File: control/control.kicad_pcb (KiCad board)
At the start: 4 copper layers, 45.7 x 39.4 mm, 90 parts, among them M1 LMR62014, M2 LM46001, M3 STM32F4XX, M4 TPS736XX, M5 SN65HVD23X, P1 GND/VDD, P2 VOLTAGE, P3 INTERFACE, P4 POWER/FETS, P5 SENSOR_A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

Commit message: Added separate +5v polygon on control board.
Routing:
- net +5V: track 67.3 -> 71.3 mm, vias 1 -> 5
- net +3.3V: track 72.8 -> 70.7 mm, vias 15 -> 14
- added copper zone on In2.Cu, net +5V
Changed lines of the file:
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@@
     (links 215)
     (no_connects 0)
-    (area 96.4311 52.395 155.955 99.770001)
+    (area 97.079999 60.249999 142.950001 99.770001)
     (thickness 1.6)
     (drawings 7)
-    (tracks 718)
+    (tracks 723)
     (zones 0)
     (modules 90)
@@
   (title_block
     (title "Phobia Control Board")
-    (date 2016-03-25)
+    (date 2016-03-31)
     (rev 2)
     (company "Roman Belov")
@@
   )
   (setup
-    (last_trace_width 1.016)
+    (last_trace_width 0.889)
     (user_trace_width 0.381)
     (user_trace_width 0.508)
@@
       (net 72 EN_A))
   )
-  (gr_text r2 (at 108.585 97.155) (layer B.Cu)
-    (effects (font (size 1.5 1.5) (thickness 0.3)) (justify mirror))
+  (gr_text r2 (at 116.205 82.55 360) (layer F.Cu)
+    (effects (font (size 1.5 1.5) (thickness 0.3)))
   )
   (dimension 39.37 (width 0.3) (layer Eco1.User)
@@
   (gr_line (start 142.875 60.325) (end 142.875 99.695) (layer Edge.Cuts) (width 0.15))
   (gr_line (start 97.155 60.325) (end 142.875 60.325) (layer Edge.Cuts) (width 0.15))
+  (segment (start 111.76 81.28) (end 106.68 81.28) (width 0.889) (layer F.Cu) (net 1))
+  (segment (start 111.76 81.28) (end 111.76 78.867) (width 0.889) (layer F.Cu) (net 1))
+  (segment (start 112.395 81.28) (end 111.76 81.28) (width 0.889) (layer F.Cu) (net 1))
+  (via (at 111.76 81.28) (size 0.7) (drill 0.3) (layers F.Cu B.Cu) (net 1))
+  (segment (start 113.03 81.28) (end 112.395 81.28) (width 0.889) (layer F.Cu) (net 1))
+  (via (at 112.395 81.28) (size 0.7) (drill 0.3) (layers F.Cu B.Cu) (net 1))
+  (segment (start 113.665 81.28) (end 113.03 81.28) (width 0.889) (layer F.Cu) (net 1))
+  (via (at 113.03 81.28) (size 0.7) (drill 0.3) (layers F.Cu B.Cu) (net 1))
+  (segment (start 113.792 78.74) (end 113.792 81.153) (width 0.889) (layer F.Cu) (net 1))
+  (segment (start 113.792 81.153) (end 113.665 81.28) (width 0.889) (layer F.Cu) (net 1))
+  (via (at 113.665 81.28) (size 0.7) (drill 0.3) (layers F.Cu B.Cu) (net 1))
+  (segment (start 111.76 78.867) (end 111.633 78.74) (width 0.889) (layer F.Cu) (net 1))
   (segment (start 102.235 83.312) (end 100.457 83.312) (width 0.889) (layer B.Cu) (net 1))
   (segment (start 100.457 83.312) (end 100.33 83.185) (width 0.889) (layer B.Cu) (net 1))
@@
   (segment (start 100.035001 71.079001) (end 103.018201 71.079001) (width 0.508) (layer F.Cu) (net 1))
   (segment (start 103.155 70.942202) (end 103.155 70.125) (width 0.508) (layer F.Cu) (net 1))
-  (segment (start 106.68 81.28) (end 111.506 81.28) (width 0.889) (layer F.Cu) (net 1))
-  (segment (start 111.633 81.153) (end 111.633 78.74) (width 0.889) (layer F.Cu) (net 1))
-  (segment (start 111.506 81.28) (end 111.633 81.153) (width 0.889) (layer F.Cu) (net 1))
   (segment (start 101.6 82.9945) (end 101.6 81.28) (width 0.889) (layer F.Cu) (net 1))
   (segment (start 101.6 81.28) (end 106.68 81.28) (width 0.889) (layer F.Cu) (net 1))
@@
   (segment (start 100.5205 82.9945) (end 100.33 83.185) (width 1.016) (layer F.Cu) (net 1))
   (segment (start 99.06 81.28) (end 101.6 81.28) (width 0.889) (layer F.Cu) (net 1))
-  (segment (start 111.633 79.502) (end 111.633 78.74) (width 0.889) (layer F.Cu) (net 1))
   (segment (start 98.288499 80.508499) (end 99.06 81.28) (width 0.889) (layer F.Cu) (net 1))
   (segment (start 99.695 70.739) (end 99.5045 70.739) (width 0.889) (layer F.Cu) (net 1))
@@
   (segment (start 127.4445 78.74) (end 127.4445 80.01) (width 0.508) (layer B.Cu) (net 3))
   (segment (start 127.4445 80.01) (end 128.0795 80.645) (width 0.508) (layer B.Cu) (net 3))
-  (via (at 114.3 83.185) (size 0.7) (drill 0.3) (layers F.Cu B.Cu) (net 3))
-  (segment (start 113.792 83.693) (end 114.3 83.185) (width 0.508) (layer B.Cu) (net 3))
-  (segment (start 113.792 85.09) (end 113.792 83.693) (width 0.508) (layer B.Cu) (net 3))
   (segment (start 135.89 95.6945) (end 135.89 94.615) (width 0.508) (layer F.Cu) (net 3))
   (via (at 135.89 94.615) (size 0.7) (drill 0.3) (layers F.Cu B.Cu) (net 3))
@@
   (via (at 115.57 80.01) (size 0.7) (drill 0.3) (layers F.Cu B.Cu) (net 61))
   (segment (start 109.855 78.105) (end 109.855 77.47) (width 0.508) (layer F.Cu) (net 61))
-  (via (at 109.855 77.47) (size 0.7) (drill 0.3) (layers F.Cu B.Cu) (net 61))
-  (segment (start 109.855 78.74) (end 109.855 78.105) (width 0.508) (layer B.Cu) (net 61))
-  (via (at 109.855 78.105) (size 0.7) (drill 0.3) (layers F.Cu B.Cu) (net 61))
-  (segment (start 109.855 79.375) (end 109.855 78.74) (width 0.508) (layer F.Cu) (net 61))
-  (via (at 109.855 78.74) (size 0.7) (drill 0.3) (layers F.Cu B.Cu) (net 61))
-  (segment (start 109.855 80.01) (end 109.855 79.375) (width 0.508) (layer B.Cu) (net 61))
-  (via (at 109.855 79.375) (size 0.7) (drill 0.3) (layers F.Cu B.Cu) (net 61))
-  (segment (start 108.585 78.74) (end 109.855 80.01) (width 0.508) (layer F.Cu) (net 61))
   (via (at 109.855 80.01) (size 0.7) (drill 0.3) (layers F.Cu B.Cu) (net 61))
+  (segment (start 108.585 78.74) (end 109.855 80.01) (width 0.508) (layer F.Cu) (net 61))
+  (via (at 109.855 79.375) (size 0.7) (drill 0.3) (layers F.Cu B.Cu) (net 61))
+  (segment (start 109.855 80.01) (end 109.855 79.375) (width 0.508) (layer B.Cu) (net 61))
+  (via (at 109.855 78.74) (size 0.7) (drill 0.3) (layers F.Cu B.Cu) (net 61))
+  (segment (start 109.855 79.375) (end 109.855 78.74) (width 0.508) (layer F.Cu) (net 61))
+  (via (at 109.855 78.105) (size 0.7) (drill 0.3) (layers F.Cu B.Cu) (net 61))
+  (segment (start 109.855 78.74) (end 109.855 78.105) (width 0.508) (layer B.Cu) (net 61))
+  (via (at 109.855 77.47) (size 0.7) (drill 0.3) (layers F.Cu B.Cu) (net 61))
   (segment (start 109.855 74.295) (end 109.855 73.66) (width 0.508) (layer F.Cu) (net 61))
   (via (at 109.855 73.66) (size 0.7) (drill 0.3) (layers F.Cu B.Cu) (net 61))
@@
     (polygon
       (pts
-        (xy 114.935 67.945) (xy 116.84 67.945) (xy 116.84 70.485) (xy 114.3 73.025) (xy 114.3 80.645)
-        (xy 111.125 80.645) (xy 111.125 72.39) (xy 114.935 68.58)
+        (xy 114.935 67.945) (xy 116.84 67.945) (xy 116.84 70.485) (xy 114.3 73.025) (xy 114.3 81.915)
+        (xy 111.125 81.915) (xy 111.125 72.39) (xy 114.935 68.58)
       )
     )
@@
       )
     )
+  )
+  (zone (net 1) (net_name +5V) (layer In2.Cu) (hatch edge 0.508)
+    (priority 1)
+    (connect_pads (clearance 0.254))
+    (min_thickness 0.254)
+    (fill yes (arc_segments 16) (thermal_gap 0.508) (thermal_bridge_width 0.508))
+    (polygon
+      (pts
+        (xy 97.79 60.96) (xy 109.22 60.96) (xy 118.11 69.85) (xy 118.11 81.28) (xy 114.3 85.09)
+        (xy 107.95 85.09) (xy 106.68 86.36) (xy 106.68 92.329) (xy 103.886 95.123) (xy 103.886 99.06)
+        (xy 97.79 99.06)
+      )
+    )

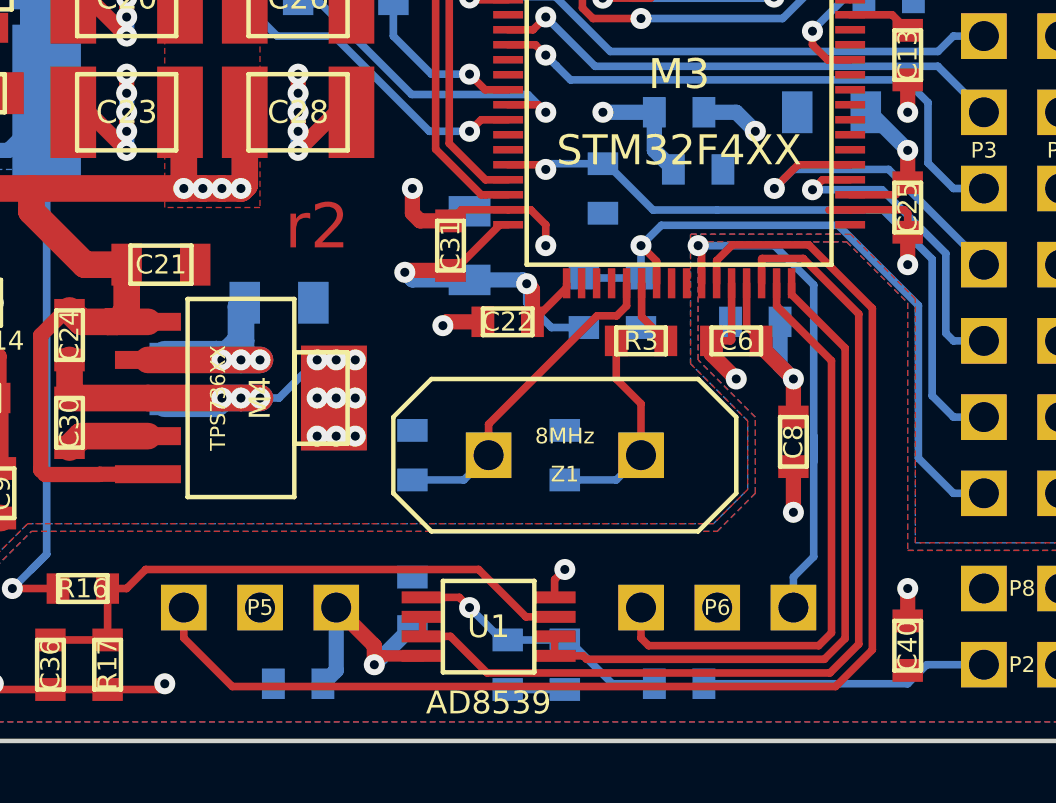
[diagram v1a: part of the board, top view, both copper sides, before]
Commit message: Replaced ACS7XX sensors to the current shunt amplifiers.
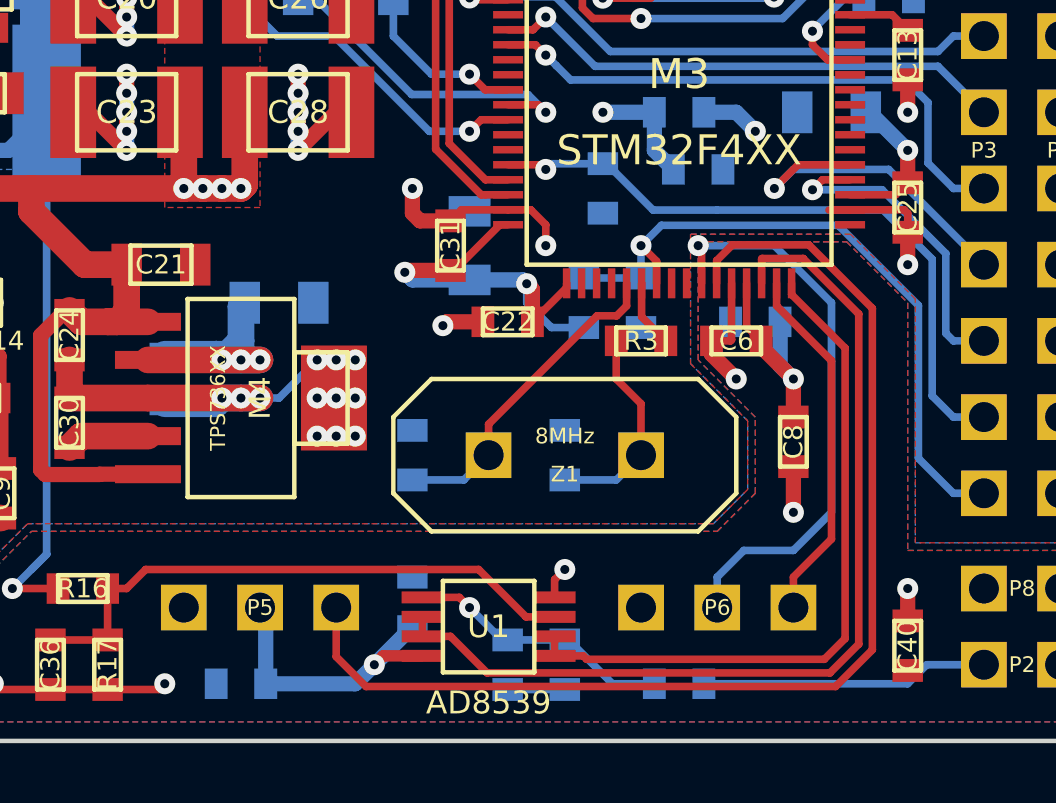
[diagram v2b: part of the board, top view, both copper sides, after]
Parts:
- moved C43 1.90 mm to (113.7, 97.8)
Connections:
- P5 pad 1: ADC_IN13 -> GND
- P5 pad 2: GND -> +3.3V
- P5 pad 3: +3.3V -> ADC_IN13
- P6 pad 1: ADC_IN1 -> GND
- P6 pad 2: GND -> ADC_IN12
- P6 pad 3: ADC_IN12 -> ADC_IN1
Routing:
- net ADC_IN1: track 20.1 -> 12.1 mm
- net ADC_IN13: track 43.6 -> 39.1 mm
- net ADC_IN12: track 17.6 -> 19.2 mm
- net +3.3V: track 70.7 -> 72.0 mm
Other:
- board text removed: "r2"
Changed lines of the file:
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@@
-(kicad_pcb (version 4) (host pcbnew 4.0.1-stable)
+(kicad_pcb (version 4) (host pcbnew 4.0.2-stable)
   (general
     (links 215)
@@
     (area 97.079999 60.249999 142.950001 99.770001)
     (thickness 1.6)
-    (drawings 7)
-    (tracks 723)
+    (drawings 6)
+    (tracks 722)
     (zones 0)
     (modules 90)
@@
   )
   (setup
-    (last_trace_width 0.889)
+    (last_trace_width 0.508)
     (user_trace_width 0.381)
     (user_trace_width 0.508)
@@
     )
     (pad 1 thru_hole rect (at -2.54 0) (size 1.524 1.524) (drill 1) (layers *.Cu *.Mask)
+      (net 61 GND))
+    (pad 3 thru_hole rect (at 2.54 0) (size 1.524 1.524) (drill 1) (layers *.Cu *.Mask)
       (net 68 ADC_IN13))
-    (pad 3 thru_hole rect (at 2.54 0) (size 1.524 1.524) (drill 1) (layers *.Cu *.Mask)
-      (net 3 +3.3V))
     (pad 2 thru_hole rect (at 0 0) (size 1.524 1.524) (drill 1) (layers *.Cu *.Mask)
-      (net 61 GND))
+      (net 3 +3.3V))
   )
   (module foot:PLS3 (layer F.Cu)
@@
     )
     (pad 1 thru_hole rect (at -2.54 0) (size 1.524 1.524) (drill 1) (layers *.Cu *.Mask)
+      (net 61 GND))
+    (pad 3 thru_hole rect (at 2.54 0) (size 1.524 1.524) (drill 1) (layers *.Cu *.Mask)
       (net 32 ADC_IN1))
-    (pad 3 thru_hole rect (at 2.54 0) (size 1.524 1.524) (drill 1) (layers *.Cu *.Mask)
+    (pad 2 thru_hole rect (at 0 0) (size 1.524 1.524) (drill 1) (layers *.Cu *.Mask)
       (net 70 ADC_IN12))
-    (pad 2 thru_hole rect (at 0 0) (size 1.524 1.524) (drill 1) (layers *.Cu *.Mask)
-      (net 61 GND))
   )
   (module foot:PLS2 (layer F.Cu)
@@
   )
   (module foot:SM0603 (layer B.Cu)
-    (at 115.57 97.79 180)
+    (at 113.665 97.79 180)
     (attr smd)
     (fp_text reference C43 (at 0 0 180) (layer B.SilkS)
@@
     (pad 2 thru_hole rect (at -8.89 0 270) (size 1.524 1.524) (drill 1) (layers *.Cu *.Mask)
       (net 72 EN_A))
-  )
-  (gr_text r2 (at 116.205 82.55 360) (layer F.Cu)
-    (effects (font (size 1.5 1.5) (thickness 0.3)))
   )
   (dimension 39.37 (width 0.3) (layer Eco1.User)
@@
   (segment (start 109.22 65.151) (end 109.22 62.23) (width 1.016) (layer B.Cu) (net 2))
   (segment (start 107.188 67.183) (end 109.22 65.151) (width 1.016) (layer B.Cu) (net 2))
+  (segment (start 114.4905 97.79) (end 117.475 97.79) (width 0.508) (layer B.Cu) (net 3))
+  (segment (start 117.475 97.79) (end 118.11 97.155) (width 0.508) (layer B.Cu) (net 3))
+  (segment (start 114.4905 97.79) (end 114.4905 95.4405) (width 0.508) (layer B.Cu) (net 3))
+  (segment (start 114.4905 95.4405) (end 114.3 95.25) (width 0.508) (layer B.Cu) (net 3))
+  (segment (start 114.4905 95.4405) (end 114.3 95.25) (width 0.508) (layer F.Cu) (net 3))
   (segment (start 127.4445 78.74) (end 127.4445 80.01) (width 0.508) (layer B.Cu) (net 3))
   (segment (start 127.4445 80.01) (end 128.0795 80.645) (width 0.508) (layer B.Cu) (net 3))
@@
   (segment (start 119.72 96.86) (end 118.405 96.86) (width 0.381) (layer F.Cu) (net 3))
   (segment (start 118.405 96.86) (end 118.11 97.155) (width 0.381) (layer F.Cu) (net 3))
-  (segment (start 118.11 97.155) (end 118.11 96.52) (width 0.508) (layer F.Cu) (net 3))
-  (segment (start 118.11 96.52) (end 116.84 95.25) (width 0.508) (layer F.Cu) (net 3))
   (segment (start 123.19 85.09) (end 123.19 84.455) (width 0.254) (layer B.Cu) (net 3))
   (segment (start 124.0155 85.9155) (end 123.19 85.09) (width 0.254) (layer B.Cu) (net 3))
@@
   (segment (start 131.6355 85.725) (end 131.6355 87.1855) (width 0.508) (layer B.Cu) (net 3))
   (segment (start 131.6355 87.1855) (end 132.08 87.63) (width 0.508) (layer B.Cu) (net 3))
-  (segment (start 116.84 95.25) (end 116.84 97.3455) (width 0.508) (layer B.Cu) (net 3))
-  (segment (start 116.84 97.3455) (end 116.3955 97.79) (width 0.508) (layer B.Cu) (net 3))
   (segment (start 113.665 86.995) (end 113.665 86.36) (width 0.889) (layer B.Cu) (net 3))
   (segment (start 113.665 86.36) (end 113.665 85.217) (width 0.889) (layer B.Cu) (net 3))
@@
   (segment (start 132.08 87.63) (end 132.08 88.9) (width 0.508) (layer F.Cu) (net 3))
   (via (at 132.08 87.63) (size 0.7) (drill 0.3) (layers F.Cu B.Cu) (net 3))
-  (segment (start 117.0305 95.0595) (end 116.84 95.25) (width 0.508) (layer F.Cu) (net 3))
   (segment (start 121.285 84.328) (end 123.063 84.328) (width 0.508) (layer B.Cu) (net 3))
   (segment (start 123.063 84.328) (end 123.19 84.455) (width 0.508) (layer B.Cu) (net 3))
@@
   (segment (start 127.8255 86.36) (end 127.02 85.5545) (width 0.254) (layer F.Cu) (net 29))
   (segment (start 127.02 85.5545) (end 127.02 84.44) (width 0.254) (layer F.Cu) (net 29))
-  (segment (start 133.35 96.092602) (end 133.35 87.024) (width 0.254) (layer F.Cu) (net 32))
-  (segment (start 133.35 87.024) (end 131.52 85.194) (width 0.254) (layer F.Cu) (net 32))
-  (segment (start 131.52 85.194) (end 131.52 84.44) (width 0.254) (layer F.Cu) (net 32))
-  (segment (start 127.254 96.52) (end 132.922602 96.52) (width 0.254) (layer F.Cu) (net 32))
-  (segment (start 132.922602 96.52) (end 133.35 96.092602) (width 0.254) (layer F.Cu) (net 32))
-  (segment (start 127 95.25) (end 127 96.266) (width 0.254) (layer F.Cu) (net 32))
-  (segment (start 127 96.266) (end 127.254 96.52) (width 0.254) (layer F.Cu) (net 32))
+  (segment (start 133.35 87.024) (end 133.35 92.964) (width 0.254) (layer F.Cu) (net 32))
+  (segment (start 133.35 92.964) (end 132.08 94.234) (width 0.254) (layer F.Cu) (net 32))
+  (segment (start 132.08 94.234) (end 132.08 95.25) (width 0.254) (layer F.Cu) (net 32))
+  (segment (start 131.52 84.44) (end 131.52 85.194) (width 0.254) (layer F.Cu) (net 32))
+  (segment (start 131.52 85.194) (end 133.35 87.024) (width 0.254) (layer F.Cu) (net 32))
   (segment (start 124.12 96.86) (end 124.12 96.21) (width 0.254) (layer F.Cu) (net 33))
   (segment (start 133.80401 96.280659) (end 133.110659 96.974009) (width 0.254) (layer F.Cu) (net 33))
@@
   (segment (start 126.0475 97.79) (end 124.587 96.3295) (width 0.254) (layer B.Cu) (net 67))
   (segment (start 124.587 96.3295) (end 124.46 96.3295) (width 0.254) (layer B.Cu) (net 67))
-  (segment (start 111.76 95.25) (end 111.76 96.266) (width 0.254) (layer F.Cu) (net 68))
-  (segment (start 111.76 96.266) (end 113.37603 97.88203) (width 0.254) (layer F.Cu) (net 68))
-  (segment (start 113.37603 97.88203) (end 133.486772 97.88203) (width 0.254) (layer F.Cu) (net 68))
-  (segment (start 133.486772 97.88203) (end 134.71203 96.656772) (width 0.254) (layer F.Cu) (net 68))
-  (segment (start 134.71203 96.656772) (end 134.71203 85.276361) (width 0.254) (layer F.Cu) (net 68))
-  (segment (start 134.71203 85.276361) (end 132.594658 83.158989) (width 0.254) (layer F.Cu) (net 68))
-  (segment (start 132.594658 83.158989) (end 130.047011 83.158989) (width 0.254) (layer F.Cu) (net 68))
-  (segment (start 130.047011 83.158989) (end 129.52 83.686) (width 0.254) (layer F.Cu) (net 68))
-  (segment (start 129.52 83.686) (end 129.52 84.44) (width 0.254) (layer F.Cu) (net 68))
+  (segment (start 133.486773 97.882029) (end 117.835067 97.882029) (width 0.254) (layer F.Cu) (net 68))
+  (segment (start 117.835067 97.882029) (end 116.84 96.886962) (width 0.254) (layer F.Cu) (net 68))
+  (segment (start 116.84 96.886962) (end 116.84 95.25) (width 0.254) (layer F.Cu) (net 68))
+  (segment (start 134.71203 85.276361) (end 134.71203 96.656773) (width 0.254) (layer F.Cu) (net 68))
+  (segment (start 134.71203 96.656773) (end 133.486773 97.882029) (width 0.254) (layer F.Cu) (net 68))
+  (segment (start 129.52 84.44) (end 129.52 83.686) (width 0.254) (layer F.Cu) (net 68))
+  (segment (start 129.52 83.686) (end 130.047011 83.158989) (width 0.254) (layer F.Cu) (net 68))
+  (segment (start 130.047011 83.158989) (end 132.594658 83.158989) (width 0.254) (layer F.Cu) (net 68))
+  (segment (start 132.594658 83.158989) (end 134.71203 85.276361) (width 0.254) (layer F.Cu) (net 68))
+  (segment (start 117.0305 95.0595) (end 116.84 95.25) (width 0.508) (layer F.Cu) (net 68))
   (segment (start 135.89 97.79) (end 136.525 97.155) (width 0.254) (layer B.Cu) (net 69))
   (segment (start 136.525 97.155) (end 138.43 97.155) (width 0.254) (layer B.Cu) (net 69))
   (segment (start 129.0955 97.79) (end 135.89 97.79) (width 0.254) (layer B.Cu) (net 69))
-  (segment (start 132.757001 89.535) (end 132.757001 90.396037) (width 0.254) (layer B.Cu) (net 70))
-  (segment (start 132.757001 84.497001) (end 132.757001 89.535) (width 0.254) (layer B.Cu) (net 70))
-  (segment (start 132.08 94.234) (end 132.08 95.25) (width 0.254) (layer B.Cu) (net 70))
-  (segment (start 132.757001 89.535) (end 132.757001 93.556999) (width 0.254) (layer B.Cu) (net 70))
-  (segment (start 132.757001 93.556999) (end 132.08 94.234) (width 0.254) (layer B.Cu) (net 70))
+  (segment (start 132.08 93.345) (end 130.429 93.345) (width 0.254) (layer B.Cu) (net 70))
+  (segment (start 130.429 93.345) (end 129.54 94.234) (width 0.254) (layer B.Cu) (net 70))
+  (segment (start 129.54 94.234) (end 129.54 95.25) (width 0.254) (layer B.Cu) (net 70))
+  (segment (start 133.35 92.075) (end 132.08 93.345) (width 0.254) (layer B.Cu) (net 70))
+  (segment (start 133.35 85.09) (end 133.35 92.075) (width 0.254) (layer B.Cu) (net 70))
+  (segment (start 131.445 83.185) (end 133.35 85.09) (width 0.254) (layer B.Cu) (net 70))
   (segment (start 128.905 83.185) (end 131.445 83.185) (width 0.254) (layer B.Cu) (net 70))
-  (segment (start 131.445 83.185) (end 132.757001 84.497001) (width 0.254) (layer B.Cu) (net 70))
   (segment (start 129.02 84.44) (end 129.02 83.3) (width 0.254) (layer F.Cu) (net 70))
   (segment (start 129.02 83.3) (end 128.905 83.185) (width 0.254) (layer F.Cu) (net 70))

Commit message: Small fixes for rev2.
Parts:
- moved C2 0.24 mm to (104.9, 77.9)
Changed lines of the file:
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@@
     (links 215)
     (no_connects 0)
-    (area 97.079999 60.249999 142.950001 99.770001)
+    (area 96.4311 52.395 155.955 99.770001)
     (thickness 1.6)
     (drawings 6)
@@
   (title_block
     (title "Phobia Control Board")
-    (date 2016-03-31)
+    (date 2016-09-21)
     (rev 2)
     (company "Roman Belov")
@@
   )
   (setup
-    (last_trace_width 0.508)
+    (last_trace_width 0.254)
     (user_trace_width 0.381)
     (user_trace_width 0.508)
@@
       (psnegative false)
       (psa4output false)
-      (plotreference true)
-      (plotvalue true)
+      (plotreference false)
+      (plotvalue false)
       (plotinvisibletext false)
       (padsonsilk false)
@@
   )
   (module foot:SM0805 (layer F.Cu)
-    (at 104.775 78.105)
+    (at 104.948 77.932)
     (attr smd)
     (fp_text reference C2 (at 0 0) (layer F.SilkS)
